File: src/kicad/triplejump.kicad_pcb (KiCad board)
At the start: 2 copper layers, 340 x 112 mm, 25 parts, among them M3 MountingHole_3.2mm_M3, SW1 SW_Push_45deg, SW10 SW_Push_45deg, SW11 SW_Push_45deg, SW12 SW_Push_45deg, SW13 SW_Push_45deg, SW14 SW_Push_45deg, SW15 SW_Push_45deg, SW16 SW_Push_45deg, SW17 SW_Push_45deg, SW18 SW_Push_45deg, SW19 SW_Push_45deg, SW2 SW_Push_45deg, SW20 SW_Push_45deg, SW3 SW_Push_45deg, SW4 SW_Push_45deg, SW6 SW_Push_45deg, SW7 SW_Push_45deg, SW8 SW_Push_45deg, SW9 SW_Push_45deg, U1 rp2040-zero

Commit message: Updated PCB for version 2
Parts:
- removed the SW8 at (85.8, 37.8)
- added M3: MountingHole_3.2mm_M3, MountingHole:MountingHole_3.2mm_M3, F.Cu at (207.0, 27.0)
- added M3: MountingHole_3.2mm_M3, MountingHole:MountingHole_3.2mm_M3, F.Cu at (192.0, 137.0)
- added SW1: SW_Push_45deg, Button_Switch_THT:SW_PUSH_6mm, F.Cu at (121.2, 28.9)
- moved SW16 27.1 mm to (252.1, 72.7)
- moved SW11 24.7 mm to (279.9, 88.4)
- moved SW18 20.4 mm to (289.5, 62.9)
- moved SW19 20.4 mm to (307.8, 57.3)
- moved SW17 20.4 mm to (273.0, 72.8)
- moved SW6 20.0 mm to (79.6, 49.6)
- moved SW7 20.0 mm to (98.0, 55.1)
- moved SW8 20.0 mm to (114.4, 65.1)
- moved SW12 19.6 mm to (266.1, 57.2)
- moved SW13 19.6 mm to (282.5, 47.3)
- moved SW14 19.6 mm to (300.9, 41.7)
- moved SW20 19.0 mm to (328.7, 57.3)
- moved SW15 18.6 mm to (321.7, 41.7)
- moved SW10 18.1 mm to (256.8, 121.4), turned to -48 degrees
- moved SW9 18.1 mm to (127.2, 121.4), turned to 48 degrees
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- renumbered SW1 to SW2, SW2 to SW3, SW3 to SW4, SW4 to SW5, locked to SW6, SW6 to SW7, SW7 to SW8
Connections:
- SW10 pad 1: UP -> UP2
- SW2 pad 1: S2 (START) -> S1 (SELECT)
- SW3 pad 1: S1 (SELECT) -> A1 (HOME)
- SW4 pad 1: (HOME) A1 -> A2 (CAPTURE)
- SW5 pad 1: (CAPTURE) A2 -> TURBO
- SW9 pad 1: UP -> UP1
- U1 pad 11: RIGHT -> UP2
- U1 pad 12: DOWN -> UP1
- U1 pad 13: LEFT -> RIGHT
- U1 pad 14: UP -> DOWN
- U1 pad 15: (CAPTURE) A2 -> LEFT
- U1 pad 16: (HOME) A1 -> S2 (START)
- U1 pad 18: S2 (START) -> A1 (HOME)
- U1 pad 19: RGB LED -> A2 (CAPTURE)
- U1 pad 5: (RS) R3 -> (LS) L3
- U1 pad 6: (LS) L3 -> B1 (1K)
- U1 pad 7: B1 (1K) -> (RS) R3
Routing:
- net UP: track 406.9 -> 0.00 mm
- net UP2: track 0.00 -> 109.9 mm
- net UP1: track 0.00 -> 102.4 mm
- net A1 (HOME): track 0.00 -> 43.5 mm
- net (HOME) A1: track 39.8 -> 0.00 mm
- net (LS) L3: track 109.6 -> 76.8 mm
- net A2 (CAPTURE): track 0.00 -> 31.0 mm
- net B1 (1K): track 129.9 -> 100.4 mm
- net (CAPTURE) A2: track 27.0 -> 0.00 mm
- net B3 (1P): track 110.9 -> 85.4 mm
- net B4 (2P): track 124.1 -> 98.8 mm
- net LEFT: track 134.1 -> 109.0 mm
- net DOWN: track 120.6 -> 95.5 mm
- net RIGHT: track 110.8 -> 85.7 mm
- net R1 (3P): track 141.2 -> 117.5 mm
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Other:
- board size 340 x 112 mm -> 320 x 120 mm
- board text removed: "A"
- board text removed: "B"
- board text removed: "BACK"
- board text removed: "DOWN"
- board text removed: "GUIDE"
- board text removed: "LB"
- board text removed: "LEFT"
- board text removed: "LS"
- board text removed: "LT"
- board text removed: "OTHER"
- board text removed: "RB"
- board text removed: "RIGHT"
- board text removed: "RS"
- board text removed: "RT"
- board text removed: "START"
- board text removed: "UP 1"
- board text removed: "UP 2"
- board text removed: "UP 3"
- board text removed: "X"
- board text removed: "Y"

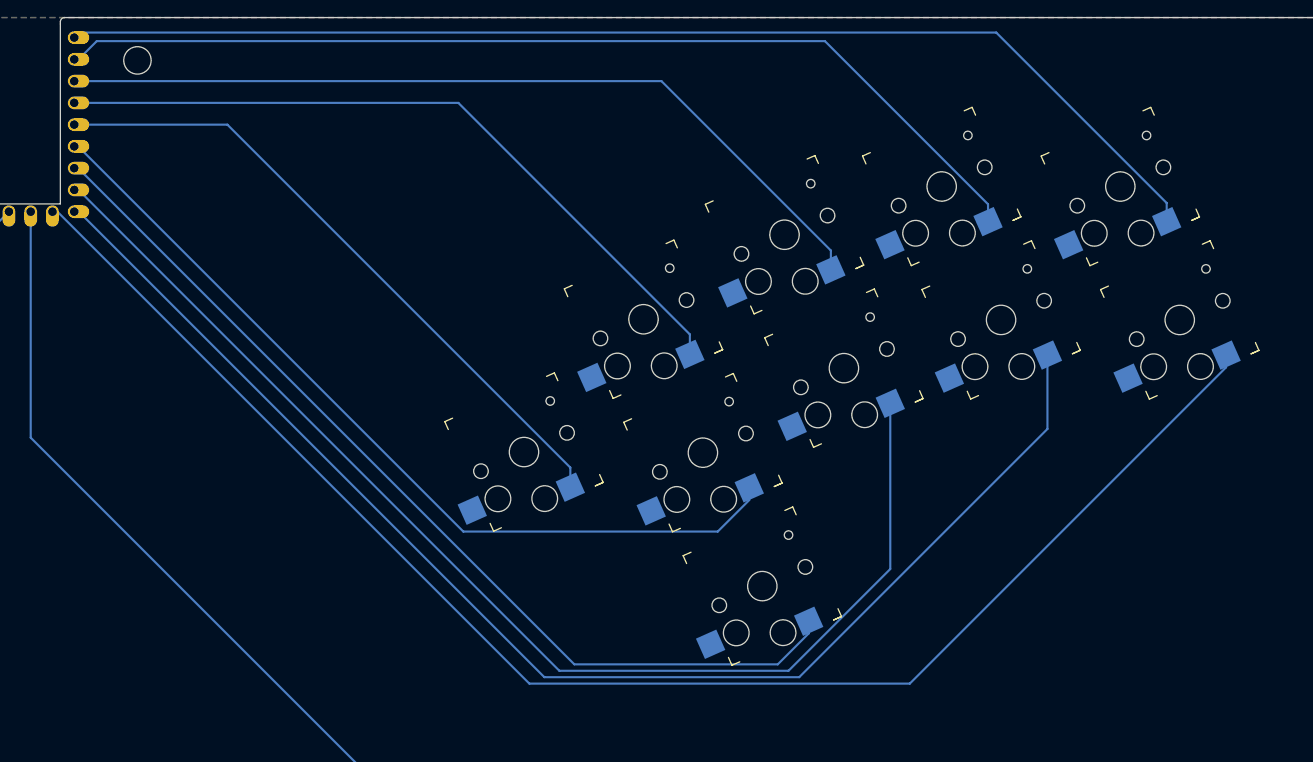
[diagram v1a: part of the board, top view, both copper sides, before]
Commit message: Fixed spacing error in right hand cluster
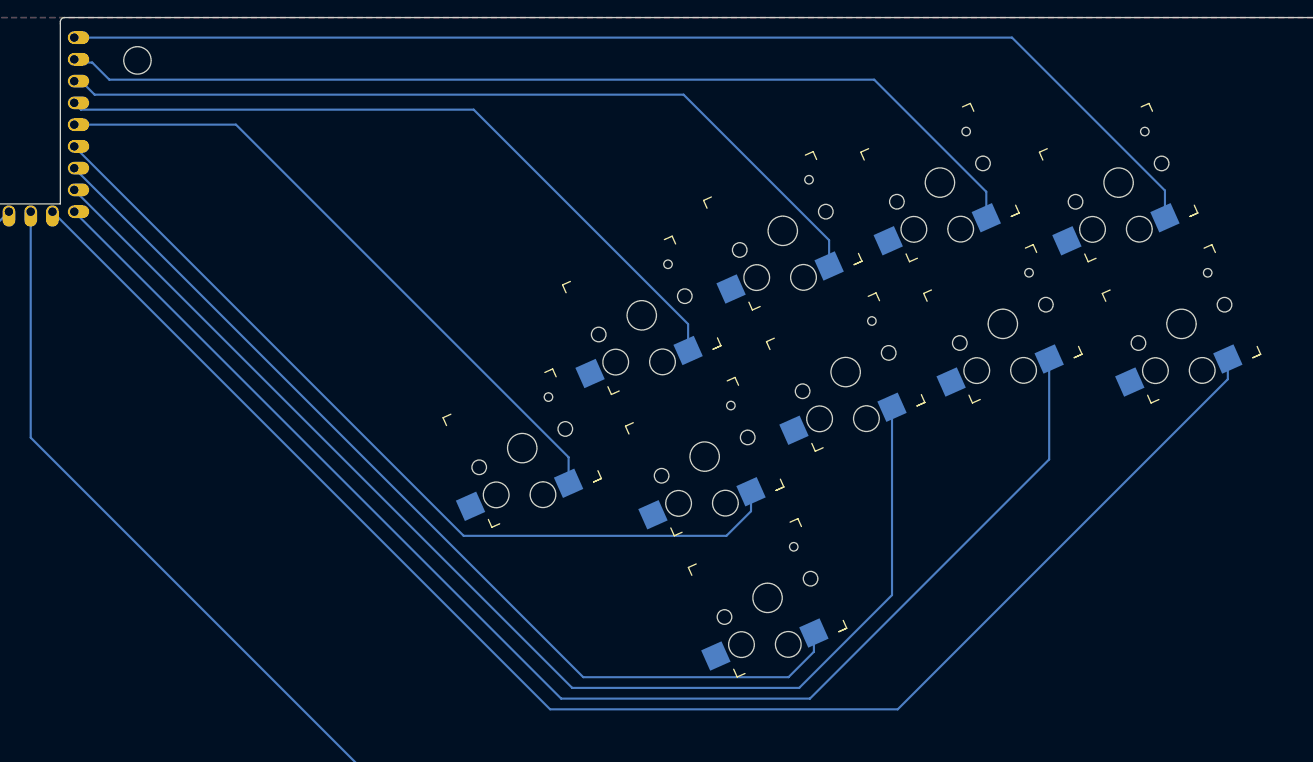
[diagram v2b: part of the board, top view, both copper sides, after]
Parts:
- moved SW11 1.50 mm to (280.6, 89.7)
- moved SW12 0.50 mm to (265.9, 56.8)
- moved SW13 0.50 mm to (282.3, 46.9)
- moved SW20 0.50 mm to (328.9, 57.8)
- moved SW14 0.50 mm to (300.7, 41.3)
- moved SW15 0.50 mm to (321.5, 41.3)
- moved SW18 0.50 mm to (289.7, 63.4)
- moved SW19 0.50 mm to (308.0, 57.8)
- moved SW16 0.50 mm to (251.9, 72.3)
- moved SW17 0.50 mm to (273.2, 73.2)
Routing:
- net R2 (3K): track 156.7 -> 160.6 mm
- net B2 (2K): track 142.8 -> 146.0 mm
- net L2 (4K): track 176.5 -> 179.6 mm
- net (RS) R3: track 112.6 -> 114.4 mm
- net R1 (3P): track 117.5 -> 115.9 mm
- net B1 (1K): track 100.4 -> 101.3 mm
